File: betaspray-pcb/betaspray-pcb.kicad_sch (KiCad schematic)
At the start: 4 parts, among them U1 ESP32-S3-WROOM-1

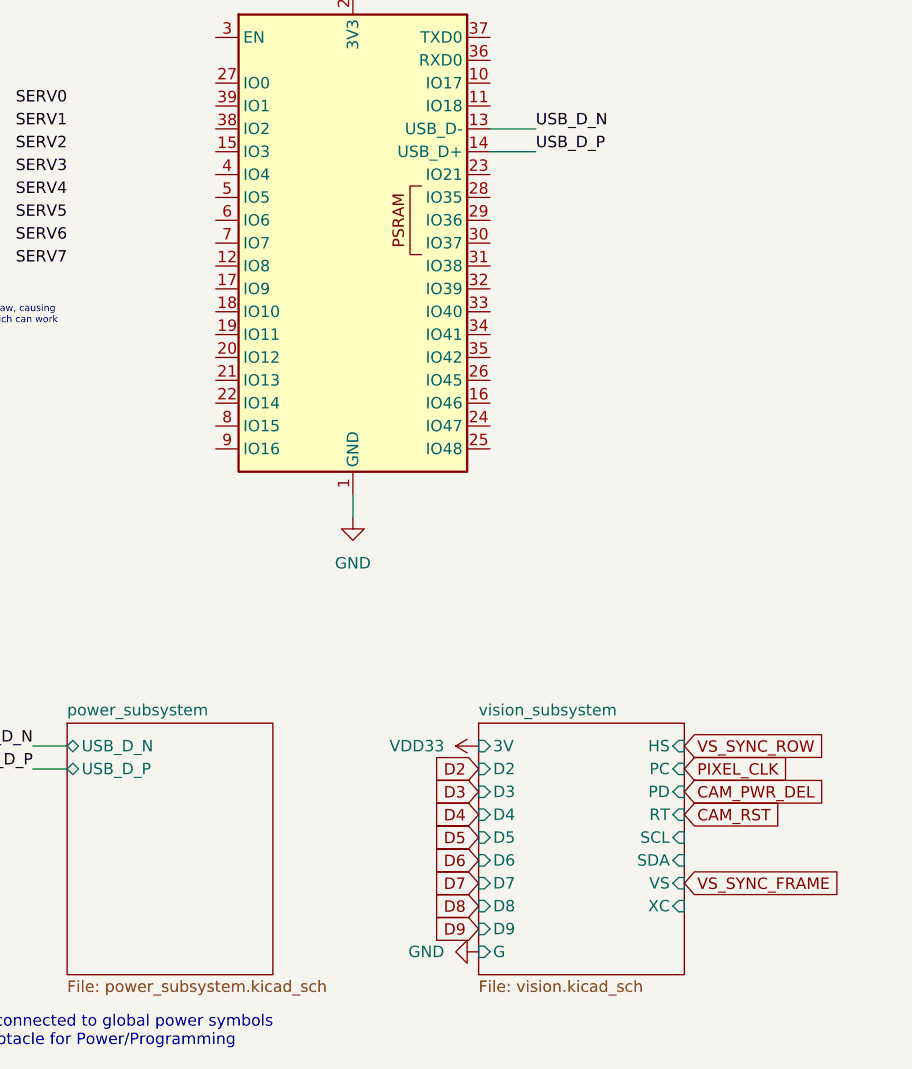
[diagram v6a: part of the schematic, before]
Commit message: pinout assignment for cam
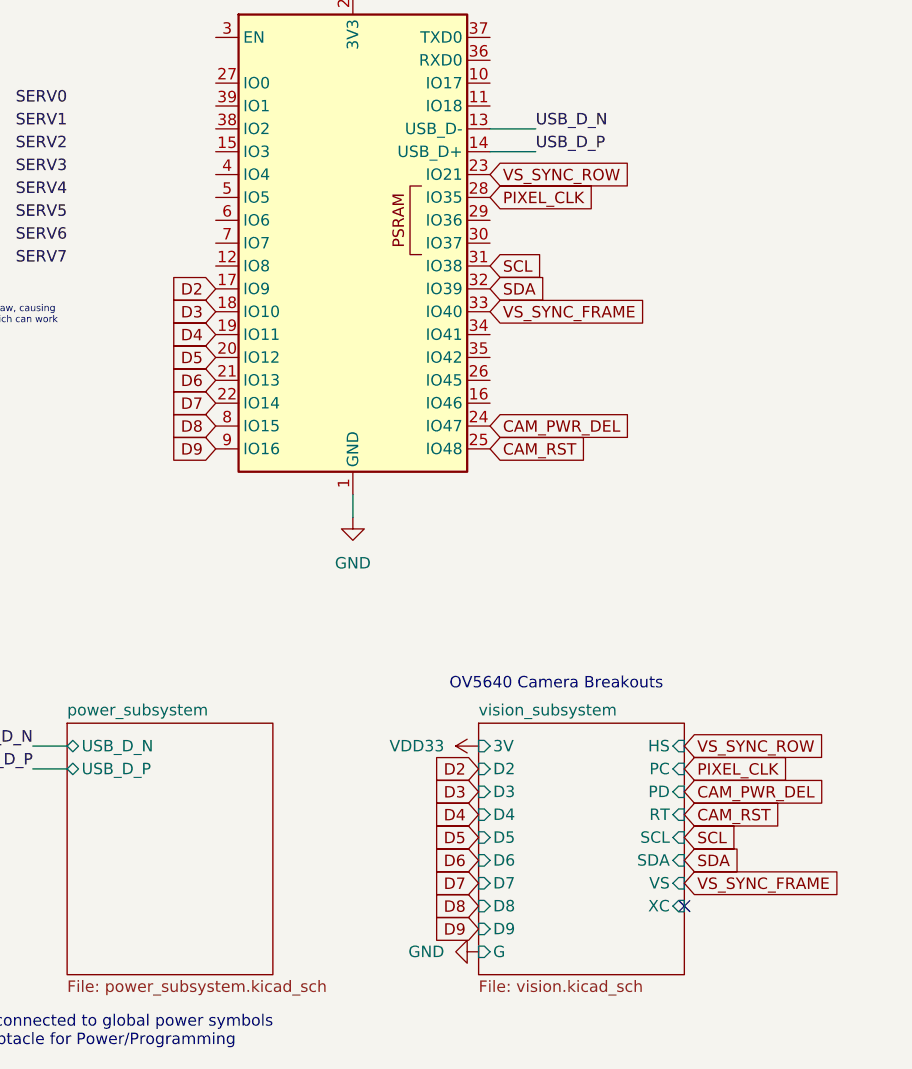
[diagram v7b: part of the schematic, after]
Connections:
- net CAM_PWR_DEL: now also U1.24 (IO47)
- net CAM_RST: now also U1.25 (IO48)
- net D2: now also U1.17 (IO9)
- net D3: now also U1.18 (IO10)
- net D4: now also U1.19 (IO11)
- net D5: now also U1.20 (IO12)
- net D6: now also U1.21 (IO13)
- net D7: now also U1.22 (IO14)
- net D8: now also U1.8 (IO15)
- net D9: now also U1.9 (IO16)
- net PIXEL_CLK: now also U1.28 (IO35)
- net VS_SYNC_FRAME: now also U1.33 (IO40)
- net VS_SYNC_ROW: now also U1.23 (IO21)
- net SCL: now reaches U1.31 (IO38)
- net SDA: now reaches U1.32 (IO39)
- no-connect marks 0 -> 1
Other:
- note added: "OV5640 Camera Breakouts"

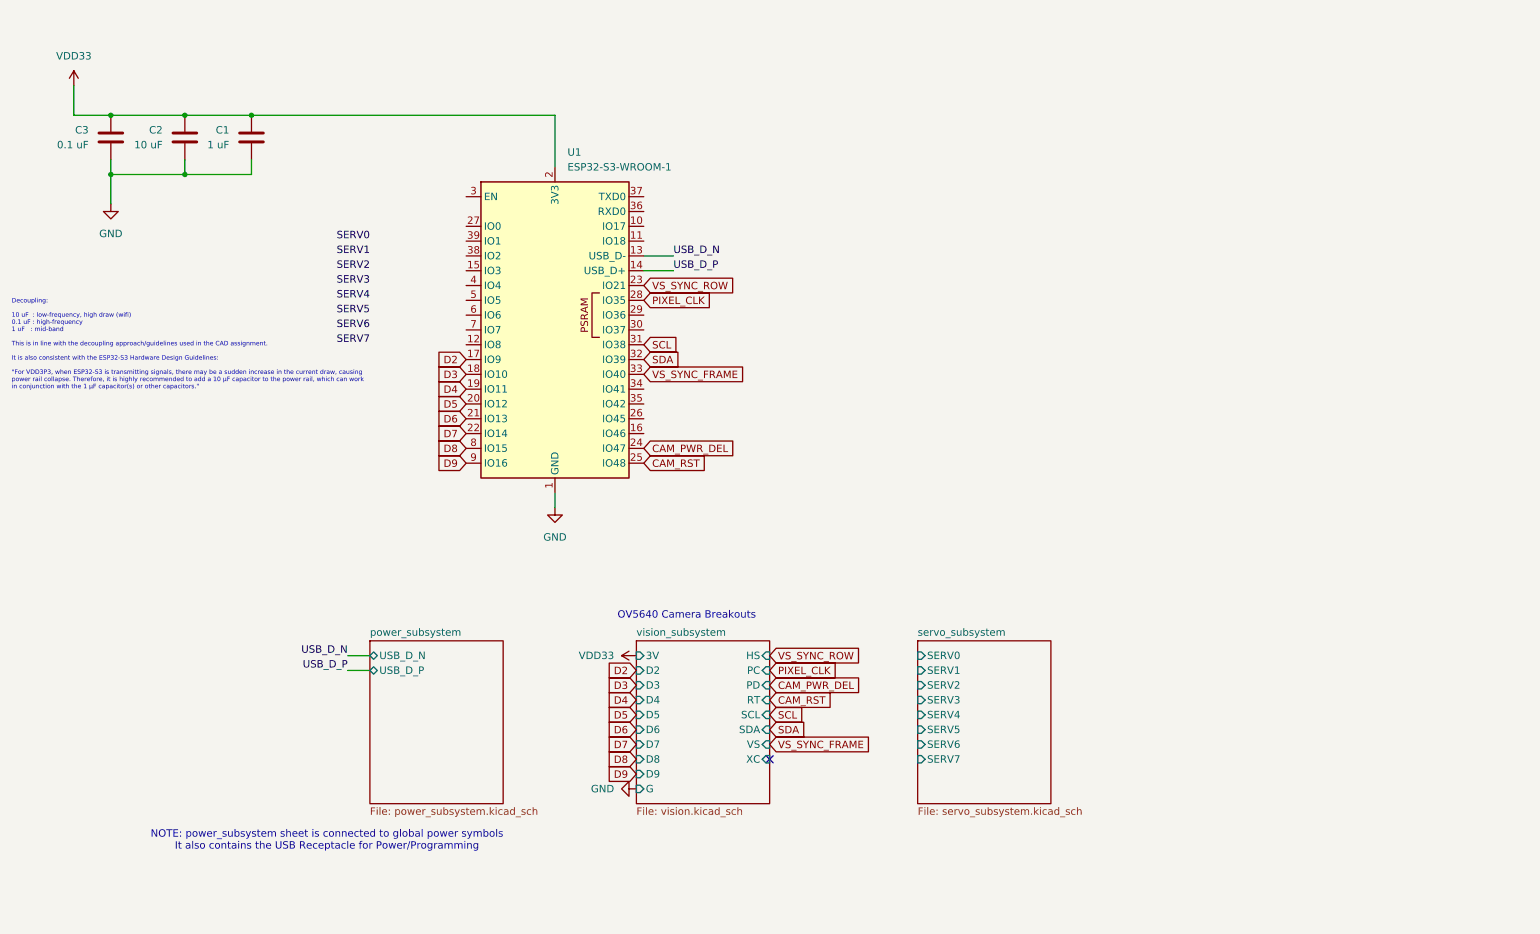
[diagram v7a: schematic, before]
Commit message: Add strapping pins
This should be correct, afaict

Still considering the automatic boot selection
via `esptool` described in:
https://docs.espressif.com/projects/esptool/en/latest/esp32s3/advanced-topics/boot-mode-selection.html#automatic-bootloader

:)
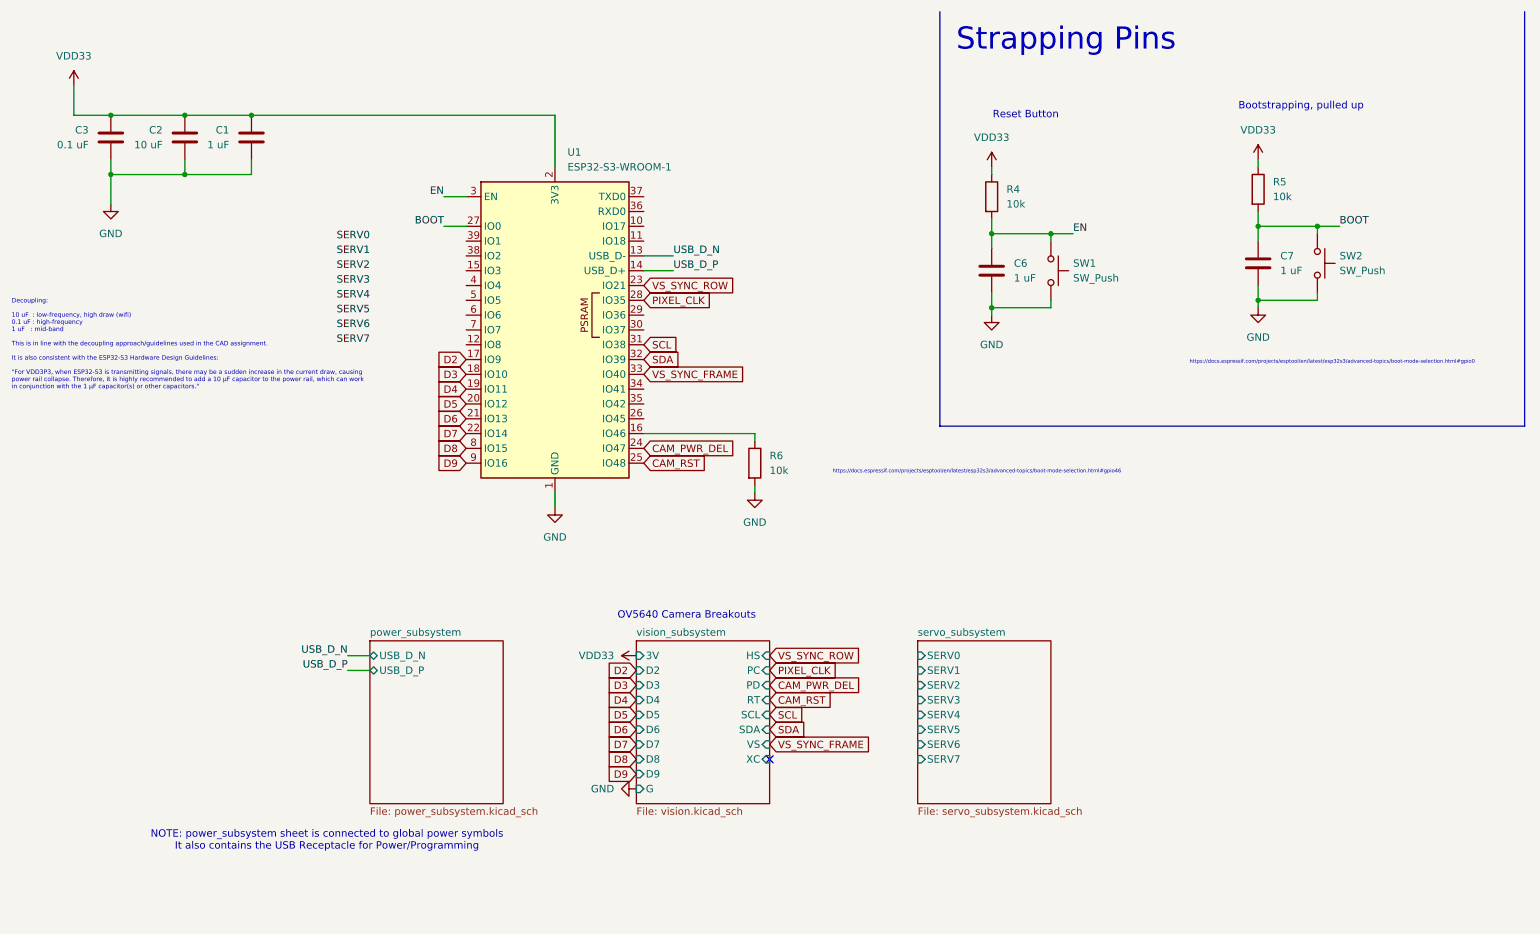
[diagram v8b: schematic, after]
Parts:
- added C6, C7: 1 uF, symbol betaspray_LDO:C
- added R4, R5, R6: 10k, symbol betaspray_LDO:R
- added SW1, SW2: SW_Push, symbol betaspray_LDO:SW_Push
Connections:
- net GND: now also C6.2, C7.2, R6.2, SW1.2, SW2.2
- net VDD33: now also R4.1, R5.1
- net at U1.16 (IO46): now also R6.1
- net BOOT: now reaches U1.27 (IO0)
- net BOOT: now also C7.1, R5.2, SW2.1
- net EN: now reaches U1.3 (EN)
- net EN: now also C6.1, R4.2, SW1.1
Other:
- note added: "Bootstrapping, pulled up"
- note added: "Reset Button"
- note added: "Strapping Pins"
- note added: "https://docs.espressif.com/projects/esptool/en/latest/esp32s3/advanced-topics/boot-mode-selection.html#gpio0"
- note added: "https://docs.espressif.com/projects/esptool/en/latest/esp32s3/advanced-topics/boot-mode-selection.html#gpio46"
